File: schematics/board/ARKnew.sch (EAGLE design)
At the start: 213 parts, among them IC2 STM32F103C8T, Q5 8MHz

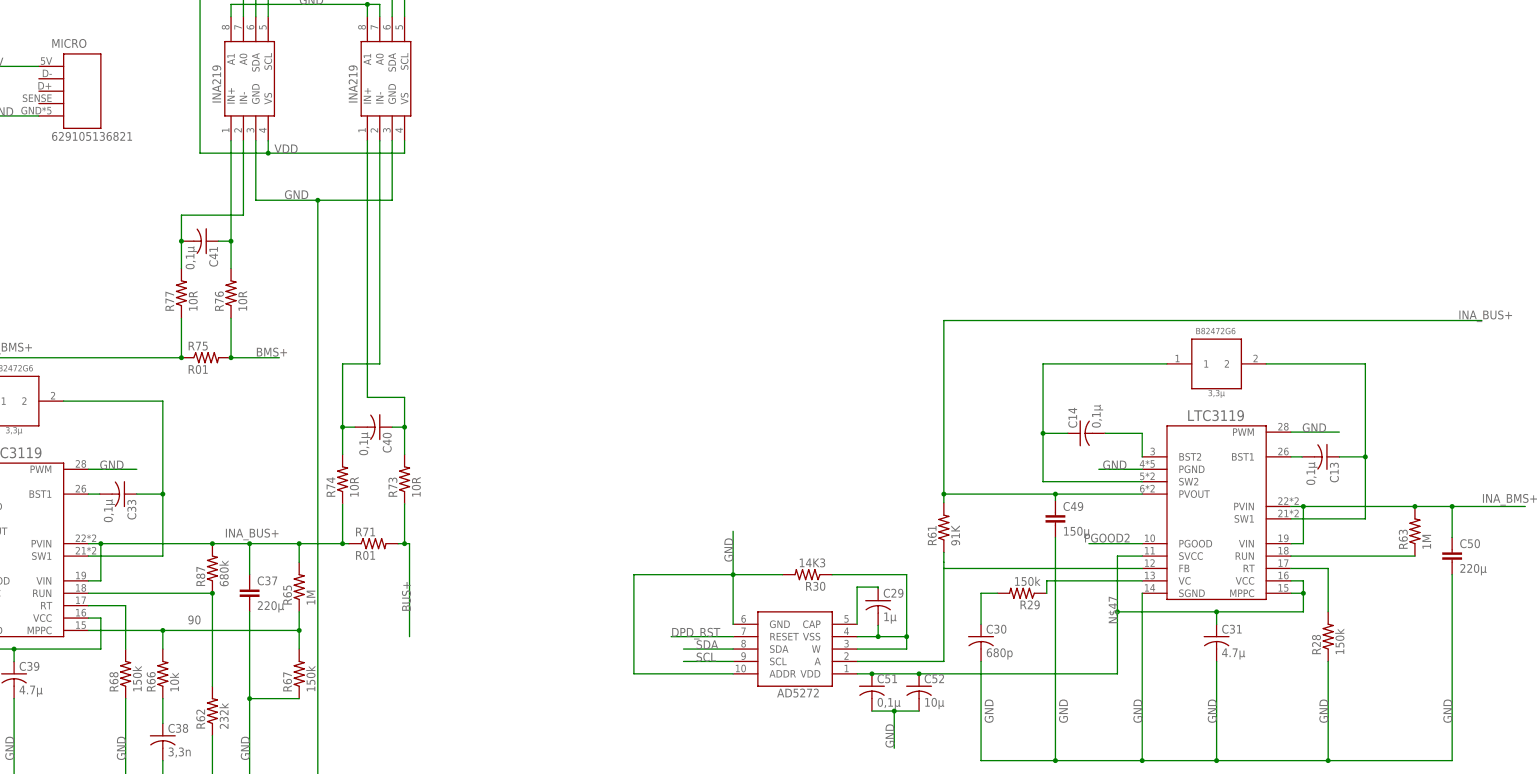
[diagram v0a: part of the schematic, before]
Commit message: Обновлена плата АРК
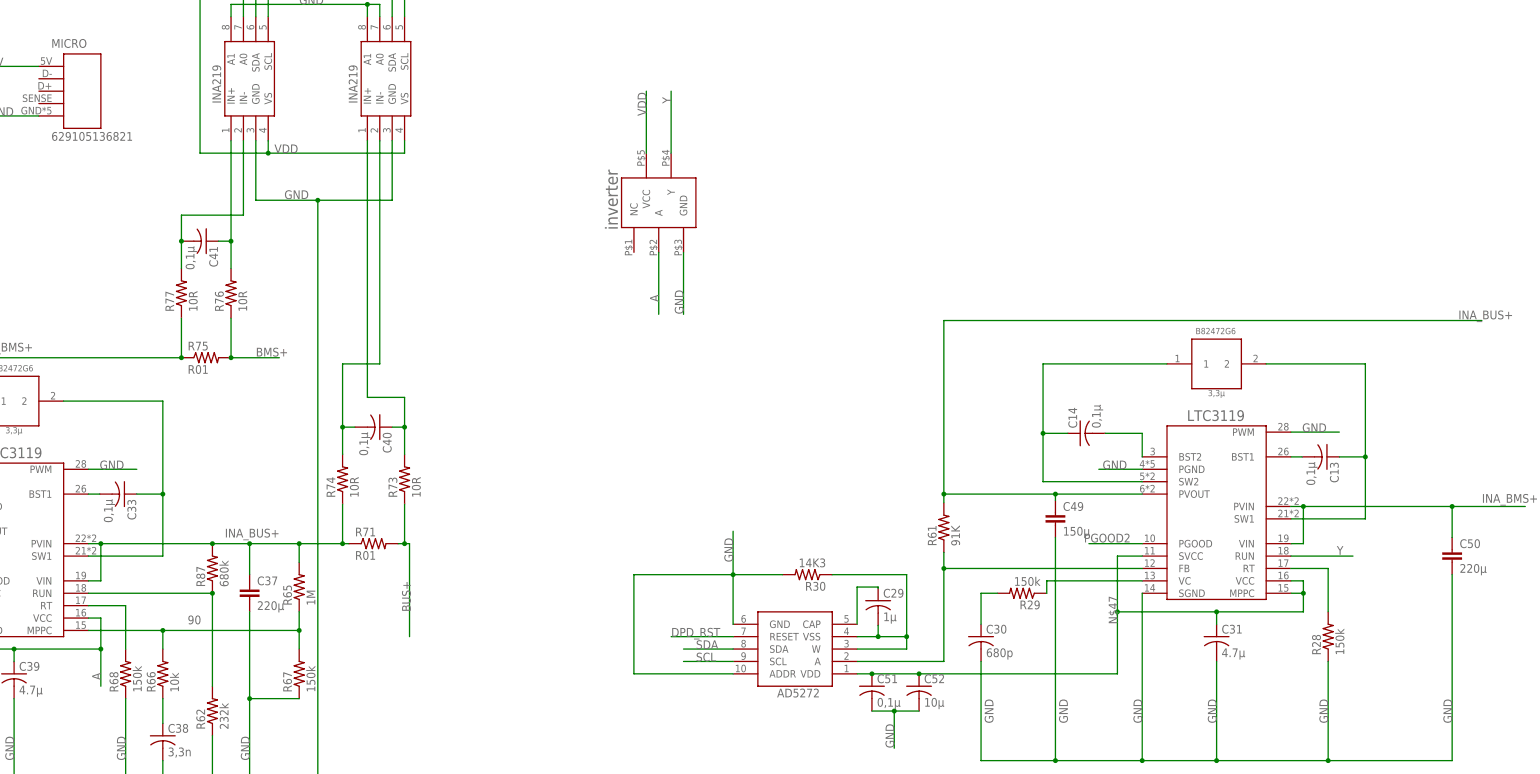
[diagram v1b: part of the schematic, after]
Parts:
- removed R63: 1M, resistor:R-US_R0603
- added U$2: INVERTER, CanCubeSat:INVERTER
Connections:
- removed net N$45: C32.1, C39.1, C43.1, U$59.SVCC, U$59.VCC, U$60.VDD
- removed net N$53: R63.1, U$16.RUN
- new net A: C32.1, C39.1, C43.1, U$2.A, U$59.SVCC, U$59.VCC, U$60.VDD
- new net Y: U$16.RUN, U$2.Y
- net GND: now also U$2.GND
- net INA_BMS+: no longer R63.2
- net VDD: now also U$2.VCC
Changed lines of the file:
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@@
 <part name="C49" library="CanCubeSat" deviceset="ECAP" device="ECAP150" value="150µ"/>
 <part name="C50" library="CanCubeSat" deviceset="ECAP" device="ECAP220" value="220µ"/>
-<part name="R63" library="resistor" library_urn="urn:adsk.eagle:library:348" deviceset="R-US_" device="R0603" package3d_urn="urn:adsk.eagle:package:23555/3" value="1M"/>
 <part name="R62" library="resistor" library_urn="urn:adsk.eagle:library:348" deviceset="R-US_" device="R0603" package3d_urn="urn:adsk.eagle:package:23555/3" value="232k"/>
 <part name="R87" library="resistor" library_urn="urn:adsk.eagle:library:348" deviceset="R-US_" device="R0603" package3d_urn="urn:adsk.eagle:package:23555/3" value="680k"/>
@@
 <part name="U$57" library="CanCubeSat" deviceset="INA219AID" device=""/>
 <part name="INA219#1" library="CanCubeSat" deviceset="INA219AID" device=""/>
+<part name="U$2" library="CanCubeSat" deviceset="INVERTER" device=""/>
 </parts>
 <sheets>
@@
 <attribute name="VALUE" x="796.544" y="137.541" size="1.778" layer="96"/>
 </instance>
-<instance part="R63" gate="G$1" x="787.4" y="146.05" smashed="yes" rot="R90">
-<attribute name="NAME" x="785.9014" y="142.24" size="1.778" layer="95" rot="R90"/>
-<attribute name="VALUE" x="790.702" y="142.24" size="1.778" layer="96" rot="R90"/>
-</instance>
 <instance part="R62" gate="G$1" x="541.02" y="109.22" smashed="yes" rot="R90">
 <attribute name="NAME" x="539.5214" y="105.41" size="1.778" layer="95" rot="R90"/>
@@
 <instance part="U$57" gate="G$1" x="548.64" y="238.76" smashed="yes" rot="R90"/>
 <instance part="INA219#1" gate="G$1" x="576.58" y="238.76" smashed="yes" rot="R90"/>
+<instance part="U$2" gate="G$1" x="632.46" y="213.36" smashed="yes"/>
 </instances>
 <busses>
@@
 <pinref part="R70" gate="G$1" pin="2"/>
 </segment>
+<segment>
+<pinref part="U$2" gate="G$1" pin="GND"/>
+<wire x1="637.54" y1="203.2" x2="637.54" y2="190.5" width="0.1524" layer="91"/>
+<label x="637.54" y="190.5" size="1.778" layer="95" rot="R90"/>
+</segment>
 </net>
 <net name="INA_BUS+" class="0">
@@
 <wire x1="795.02" y1="151.13" x2="810.006" y2="151.13" width="0.1524" layer="91"/>
 <wire x1="795.02" y1="144.78" x2="795.02" y2="151.13" width="0.1524" layer="91"/>
-<wire x1="764.54" y1="151.13" x2="787.4" y2="151.13" width="0.1524" layer="91"/>
+<wire x1="764.54" y1="151.13" x2="795.02" y2="151.13" width="0.1524" layer="91"/>
 <junction x="764.54" y="151.13"/>
 <junction x="795.02" y="151.13"/>
-<wire x1="787.4" y1="151.13" x2="795.02" y2="151.13" width="0.1524" layer="91"/>
 <pinref part="C50" gate="G$1" pin="1"/>
-<pinref part="R63" gate="G$1" pin="2"/>
-<junction x="787.4" y="151.13"/>
 </segment>
 </net>
@@
 <label x="553.72" y="223.52" size="1.778" layer="95"/>
 </segment>
+<segment>
+<pinref part="U$2" gate="G$1" pin="VCC"/>
+<wire x1="629.92" y1="223.52" x2="629.92" y2="236.22" width="0.1524" layer="91"/>
+<label x="629.92" y="231.14" size="1.778" layer="95" rot="R90"/>
+</segment>
 </net>
 <net name="N$133" class="0">
@@
 </segment>
 </net>
-<net name="N$53" class="0">
-<segment>
-<pinref part="U$16" gate="G$1" pin="RUN"/>
-<pinref part="R63" gate="G$1" pin="1"/>
-<wire x1="762" y1="140.97" x2="787.4" y2="140.97" width="0.1524" layer="91"/>
-</segment>
-</net>
 <net name="N$55" class="0">
 <segment>
@@
 <wire x1="731.52" y1="138.43" x2="690.88" y2="138.43" width="0.1524" layer="91"/>
 <pinref part="R61" gate="G$1" pin="1"/>
-<wire x1="690.88" y1="138.43" x2="690.88" y2="139.7" width="0.1524" layer="91"/>
-<wire x1="690.88" y1="139.7" x2="690.88" y2="141.732" width="0.1524" layer="91"/>
+<wire x1="690.88" y1="138.43" x2="690.88" y2="141.732" width="0.1524" layer="91"/>
 <wire x1="690.88" y1="119.38" x2="690.88" y2="138.43" width="0.1524" layer="91"/>
+<junction x="690.88" y="138.43"/>
 </segment>
 </net>
@@
 </segment>
 </net>
-<net name="N$45" class="0">
-<segment>
-<pinref part="C43" gate="G$1" pin="1"/>
-<wire x1="429.768" y1="109.22" x2="439.42" y2="109.22" width="0.1524" layer="91"/>
-<pinref part="C32" gate="G$1" pin="1"/>
-<junction x="429.768" y="109.22"/>
-<pinref part="U$60" gate="G$1" pin="VDD"/>
-<wire x1="426.72" y1="109.22" x2="429.768" y2="109.22" width="0.1524" layer="91"/>
-<pinref part="U$59" gate="G$1" pin="SVCC"/>
-<wire x1="485.14" y1="133.35" x2="480.06" y2="133.35" width="0.1524" layer="91"/>
-<wire x1="480.06" y1="133.35" x2="480.06" y2="121.92" width="0.1524" layer="91"/>
-<wire x1="480.06" y1="121.92" x2="500.38" y2="121.92" width="0.1524" layer="91"/>
-<pinref part="U$59" gate="G$1" pin="VCC"/>
-<wire x1="500.38" y1="121.92" x2="518.16" y2="121.92" width="0.1524" layer="91"/>
-<wire x1="518.16" y1="121.92" x2="518.16" y2="128.27" width="0.1524" layer="91"/>
-<wire x1="518.16" y1="128.27" x2="515.62" y2="128.27" width="0.1524" layer="91"/>
-<wire x1="500.38" y1="119.38" x2="500.38" y2="121.92" width="0.1524" layer="91"/>
-<junction x="500.38" y="121.92"/>
-<pinref part="C39" gate="G$1" pin="1"/>
-<wire x1="439.42" y1="109.22" x2="480.06" y2="109.22" width="0.1524" layer="91"/>
-<wire x1="480.06" y1="109.22" x2="480.06" y2="121.92" width="0.1524" layer="91"/>
-<junction x="439.42" y="109.22"/>
-<junction x="480.06" y="121.92"/>
-</segment>
-</net>
 <net name="N$47" class="0">
 <segment>
@@
 </segment>
 </net>
+<net name="Y" class="0">
+<segment>
+<pinref part="U$2" gate="G$1" pin="Y"/>
+<wire x1="635" y1="223.52" x2="635" y2="236.22" width="0.1524" layer="91"/>
+<label x="635" y="233.68" size="1.778" layer="95" rot="R90"/>
+</segment>
+<segment>
+<pinref part="U$16" gate="G$1" pin="RUN"/>
+<wire x1="762" y1="140.97" x2="774.7" y2="140.97" width="0.1524" layer="91"/>
+<label x="771.398" y="141.224" size="1.778" layer="95"/>
+</segment>
+</net>
+<net name="A" class="0">
+<segment>
+<pinref part="U$2" gate="G$1" pin="A"/>
+<wire x1="632.46" y1="203.2" x2="632.46" y2="190.5" width="0.1524" layer="91"/>
+<label x="632.46" y="193.04" size="1.778" layer="95" rot="R90"/>
+</segment>
+<segment>
+<pinref part="C43" gate="G$1" pin="1"/>
+<wire x1="429.768" y1="109.22" x2="439.42" y2="109.22" width="0.1524" layer="91"/>
+<pinref part="C32" gate="G$1" pin="1"/>
+<junction x="429.768" y="109.22"/>
+<pinref part="U$60" gate="G$1" pin="VDD"/>
+<wire x1="426.72" y1="109.22" x2="429.768" y2="109.22" width="0.1524" layer="91"/>
+<pinref part="U$59" gate="G$1" pin="SVCC"/>
+<wire x1="485.14" y1="133.35" x2="480.06" y2="133.35" width="0.1524" layer="91"/>
+<wire x1="480.06" y1="133.35" x2="480.06" y2="121.92" width="0.1524" layer="91"/>
+<wire x1="480.06" y1="121.92" x2="500.38" y2="121.92" width="0.1524" layer="91"/>
+<pinref part="U$59" gate="G$1" pin="VCC"/>
+<wire x1="500.38" y1="121.92" x2="518.16" y2="121.92" width="0.1524" layer="91"/>
+<wire x1="518.16" y1="121.92" x2="518.16" y2="128.27" width="0.1524" layer="91"/>
+<wire x1="518.16" y1="128.27" x2="515.62" y2="128.27" width="0.1524" layer="91"/>
+<wire x1="500.38" y1="119.38" x2="500.38" y2="121.92" width="0.1524" layer="91"/>
+<junction x="500.38" y="121.92"/>
+<pinref part="C39" gate="G$1" pin="1"/>
+<wire x1="439.42" y1="109.22" x2="480.06" y2="109.22" width="0.1524" layer="91"/>
+<wire x1="480.06" y1="109.22" x2="480.06" y2="121.92" width="0.1524" layer="91"/>
+<junction x="439.42" y="109.22"/>
+<junction x="480.06" y="121.92"/>
+<wire x1="518.16" y1="121.92" x2="518.16" y2="114.3" width="0.1524" layer="91"/>
+<junction x="518.16" y="121.92"/>
+<label x="518.16" y="115.57" size="1.778" layer="95" rot="R90"/>
+</segment>
+</net>

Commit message: АРК 2.0
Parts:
- added U$22, U$27, U$28, U$29, U$30, U$9: FS8205A-, CanCubeSat:FS8205A-
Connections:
- new net N$31: R91.2, U$9.G2
- new net N$45: R90.2, U$9.G1
- new net N$49: U$15.S1, U$22.S2
- new net N$50: U$24.S1, U$9.S2
- new net N$53: R88.2, U$22.G1
- new net N$61: R89.2, U$22.G2
- new net N$62: U$25.S1, U$27.S2
- new net N$63: R93.2, U$27.G2
- new net N$64: R92.2, U$27.G1
- new net N$73: U$28.S2, U$8.S1
- new net N$74: R97.2, U$28.G2
- new net N$77: R96.2, U$28.G1
- new net N$79: U$26.S1, U$29.S2
- new net N$80: R95.2, U$29.G2
- new net N$89: R94.2, U$29.G1
- new net N$90: U$1.S1, U$30.S2
- new net N$93: R99.2, U$30.G2
- new net N$95: R98.2, U$30.G1
- net GND: now also U$22.S1, U$27.S1, U$28.S1, U$29.S1, U$30.S1, U$9.S1; no longer U$1.S1, U$15.S1, U$24.S1, U$25.S1, U$26.S1, U$8.S1
- net OC1: no longer R95.2
- net OC2: no longer R99.2
- net OC3: no longer R93.2
- net OC4: no longer R97.2
- net OC5: no longer R91.2
- net OC6: no longer R89.2
- net OD1: no longer R94.2
- net OD2: no longer R98.2
- net OD3: no longer R92.2
- net OD4: no longer R96.2
- net OD5: no longer R90.2
- net OD6: no longer R88.2
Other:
- moved on the sheet: AB1, AB2, AB3, C1, C10, C11, C12, C17, C18, C19, C2, C20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

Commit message: Исправлены диоды в АРКе
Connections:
- net BMS+: now also LED3.A, LED4.A, LED5.A, LED6.A, LED7.A, LED8.A; no longer LED3.C, LED4.C, LED5.C, LED6.C, LED7.C, LED8.C
- net N$54: now also LED3.C; no longer LED3.A
- net N$56: now also LED4.C; no longer LED4.A
- net N$57: now also LED5.C; no longer LED5.A
- net N$58: now also LED6.C; no longer LED6.A
- net N$59: now also LED7.C; no longer LED7.A
- net N$60: now also LED8.C; no longer LED8.A
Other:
- moved on the sheet: LED3, LED4, LED5, LED6, LED7, LED8

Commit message: Изменен АРК
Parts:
- removed C32: 0,1µ, rcl:C-USC0603
- removed C42: 1µ, rcl:C-USC0603
- removed C43: 10µ, rcl:C-USC1206
- removed LED4, LED5, LED6, LED7: (no value), led:LEDCHIPLED_0603
- removed R80, R83, R84, R85, R86: 2k, resistor:R-US_R0603
- removed U$60: AD5272, CanCubeSat:AD5272
- added LED1, LED2: (no value), led:LEDCHIPLED_0603
- added R31, R32, R57: 2k, resistor:R-US_R0603
- R70: value 14k3 -> 24k3
- R72: value 91k -> 232k
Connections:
- removed net DPC_RST: IC2.PB14, U$60.RESET
- removed net N$101: R52.1, U$48.S
- removed net N$103: R53.1, U$49.S
- removed net N$154: C42.1, U$60.CAP
- removed net N$87: R45.1, U$42.S
- net A: now also LED8.A; no longer C32.1, C43.1, U$60.VDD
- net B-1: now also U$7.S; no longer R86.1, U$7.D
- net B-2: now also U$49.S; no longer R100.1, U$49.D
- net B-3: now also U$14.S; no longer R84.1, U$14.D
- net B-4: now also U$42.S; no longer R85.1, U$42.D
- net B-5: now also U$21.S; no longer R83.1, U$21.D
- net B-6: now also U$35.S; no longer R80.1, U$35.D
- net BMS+: no longer LED3.A, LED4.A, LED5.A, LED6.A, LED7.A, LED8.A
- net GND: now also R100.1, R31.1, R32.1, R57.1; no longer C32.2, C43.2, U$60.GND
- net N$10: now also U$7.D; no longer U$7.S
- net N$110: now also U$48.S; no longer U$48.D
- net N$21: now also U$13.D; no longer U$13.S
- net N$23: now also U$14.D; no longer U$14.S
- net N$25: now also R70.1; no longer U$60.A
- net N$26: now also LED1.C, R31.2; no longer C42.2, R70.1, U$60.VSS, U$60.W
- net N$30: now also U$13.S; no longer U$13.D
- net N$37: now also U$20.D; no longer U$20.S
- net N$39: now also U$21.D; no longer U$21.S
- net N$46: now also U$20.S; no longer U$20.D
- net N$47: now also LED1.A
- net N$54: now also LED2.C, R32.2; no longer LED3.C, R80.2
- net N$56: now also LED3.C, R57.2; no longer LED4.C, R83.2
- net N$57: now also R36.1, U$34.D; no longer LED5.C, R84.2
- net N$58: now also R37.1, U$35.D; no longer LED6.C, R85.2
- net N$59: now also R44.1, U$41.D; no longer LED7.C, R86.2
- net N$69: now also R45.1, U$42.D; no longer R36.1, U$34.S
- net N$7: now also U$6.D; no longer U$6.S
- net N$71: now also R52.1, U$48.D; no longer R37.1, U$35.S
- net N$78: now also U$34.S; no longer U$34.D
- net N$8: now also U$6.S; no longer U$6.D
- net N$85: now also R53.1, U$49.D; no longer R44.1, U$41.S
- net N$94: now also U$41.S; no longer U$41.D
- net PGOOD1: now also LED2.A
- net PGOOD2: now also LED3.A
- net SCL: no longer U$60.SCL
- net SDA: no longer U$60.SDA
- net VDD: no longer U$60.ADDR
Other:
- moved on the sheet: LED3, LED8, R100, R70
